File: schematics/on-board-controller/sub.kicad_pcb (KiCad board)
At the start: 2 copper layers, 90 x 60 mm, 40 parts, among them J1 5-1814832-1, J2 programmer, J3 xt60, M1 Motor_DC, M2 Motor_DC, M3 Stepper_Motor_bipolar, Q1 NMOS, Q2 NMOS, U1 L293D, U2 STM32L476RGTx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

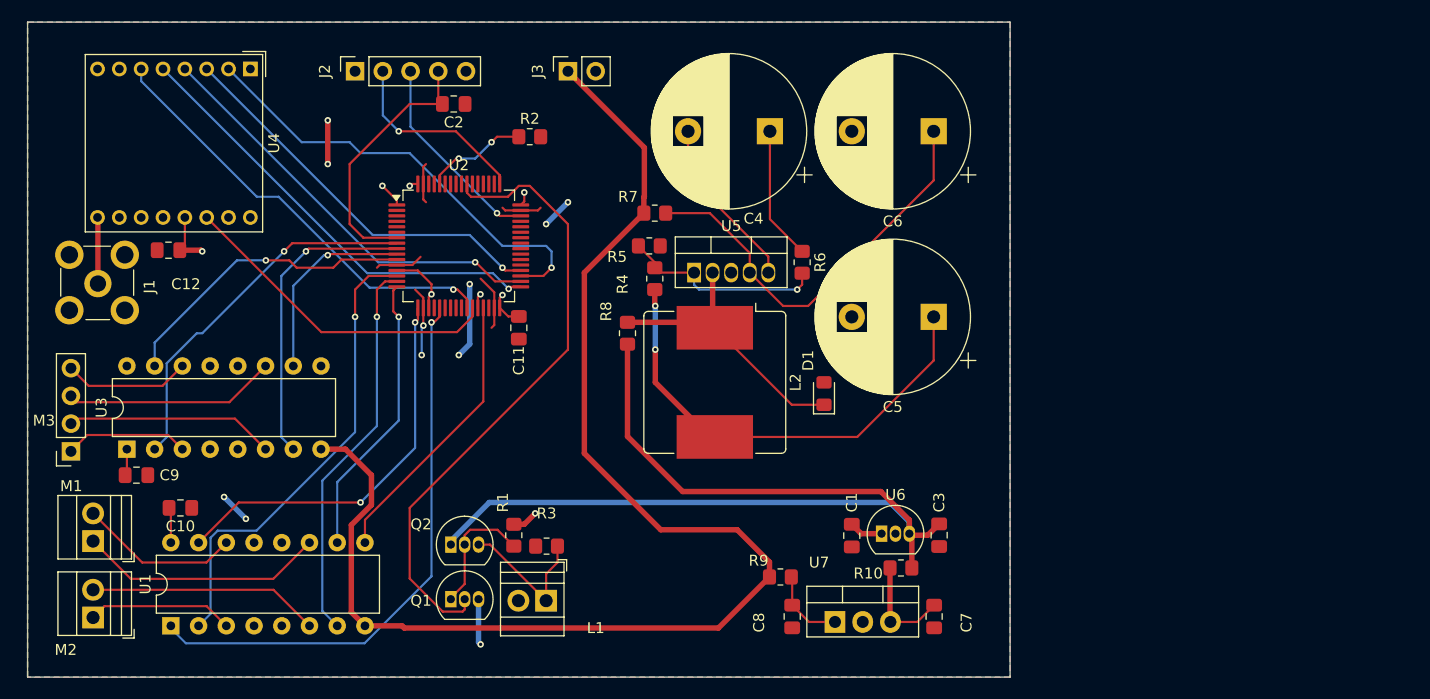
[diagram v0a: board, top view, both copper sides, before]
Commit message: new version, and ltspice for electromagnet
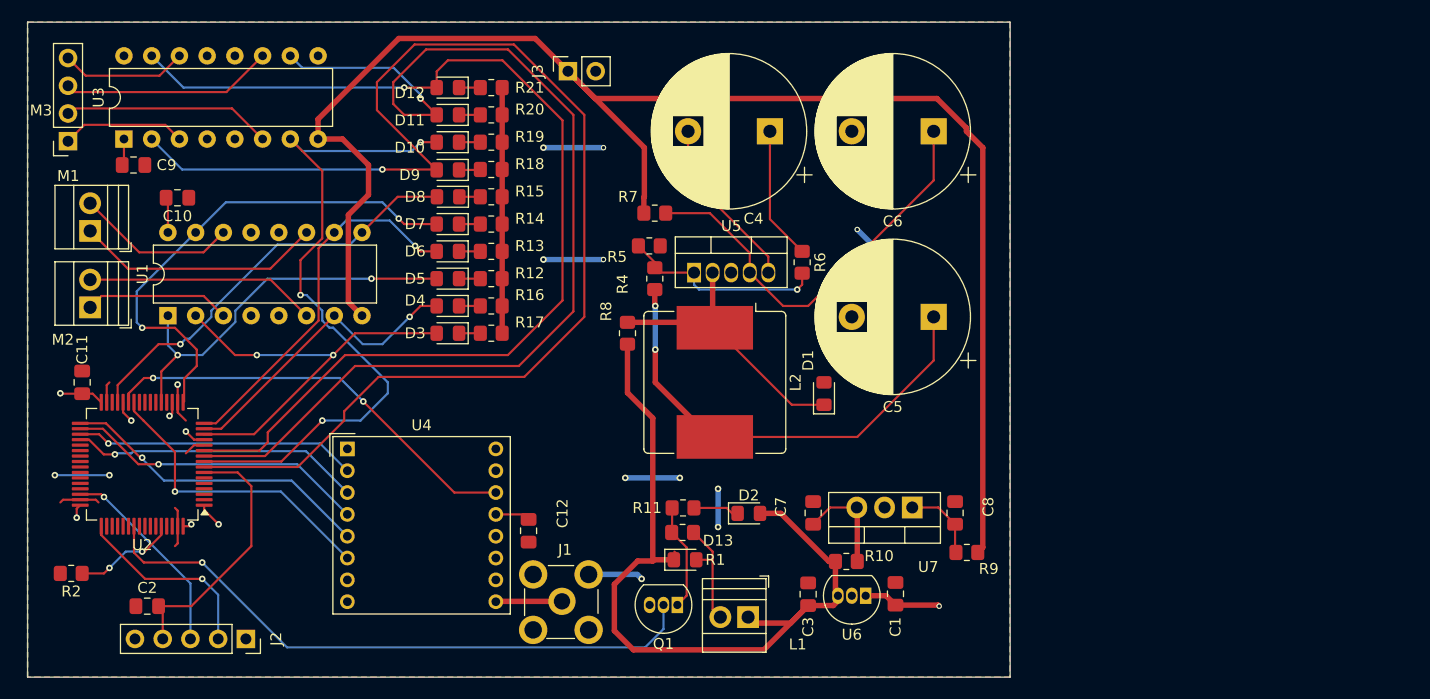
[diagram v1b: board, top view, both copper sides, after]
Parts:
- removed Q2: NMOS, Package_TO_SOT_THT:TO-92_Inline
- removed R3: 10k, Resistor_SMD:R_0805_2012Metric_Pad1.20x1.40mm_HandSolder
- added D10: LED, LED_SMD:LED_0805_2012Metric_Pad1.15x1.40mm_HandSolder, F.Cu at (101.5, 71.5)
- added D11: LED, LED_SMD:LED_0805_2012Metric_Pad1.15x1.40mm_HandSolder, F.Cu at (101.5, 69.0)
- added D12: LED, LED_SMD:LED_0805_2012Metric_Pad1.15x1.40mm_HandSolder, F.Cu at (101.5, 66.5)
- added D13: D, LED_SMD:LED_0805_2012Metric_Pad1.15x1.40mm_HandSolder, F.Cu at (123.2, 109.8)
- added D2: LED, LED_SMD:LED_0805_2012Metric_Pad1.15x1.40mm_HandSolder, F.Cu at (129.1, 105.5)
- added D3: LED, LED_SMD:LED_0805_2012Metric_Pad1.15x1.40mm_HandSolder, F.Cu at (101.5, 89.0)
- added D4: LED, LED_SMD:LED_0805_2012Metric_Pad1.15x1.40mm_HandSolder, F.Cu at (101.5, 86.5)
- added D5: LED, LED_SMD:LED_0805_2012Metric_Pad1.15x1.40mm_HandSolder, F.Cu at (101.5, 84.0)
- added D6: LED, LED_SMD:LED_0805_2012Metric_Pad1.15x1.40mm_HandSolder, F.Cu at (101.5, 81.5)
- added D7: LED, LED_SMD:LED_0805_2012Metric_Pad1.15x1.40mm_HandSolder, F.Cu at (101.5, 79.0)
- added D8: LED, LED_SMD:LED_0805_2012Metric_Pad1.15x1.40mm_HandSolder, F.Cu at (101.5, 76.5)
- added D9: LED, LED_SMD:LED_0805_2012Metric_Pad1.15x1.40mm_HandSolder, F.Cu at (101.5, 74.0)
- added R11: 330, Resistor_SMD:R_0805_2012Metric_Pad1.20x1.40mm_HandSolder, F.Cu at (123.0, 105.0)
- added R12: 330, Resistor_SMD:R_0805_2012Metric_Pad1.20x1.40mm_HandSolder, F.Cu at (105.5, 84.0)
- added R13: 330, Resistor_SMD:R_0805_2012Metric_Pad1.20x1.40mm_HandSolder, F.Cu at (105.5, 81.5)
- added R14: 330, Resistor_SMD:R_0805_2012Metric_Pad1.20x1.40mm_HandSolder, F.Cu at (105.5, 79.0)
- added R15: 330, Resistor_SMD:R_0805_2012Metric_Pad1.20x1.40mm_HandSolder, F.Cu at (105.5, 76.5)
- added R16: 330, Resistor_SMD:R_0805_2012Metric_Pad1.20x1.40mm_HandSolder, F.Cu at (105.5, 86.5)
- added R17: 330, Resistor_SMD:R_0805_2012Metric_Pad1.20x1.40mm_HandSolder, F.Cu at (105.5, 89.0)
- added R18: 330, Resistor_SMD:R_0805_2012Metric_Pad1.20x1.40mm_HandSolder, F.Cu at (105.5, 74.0)
- added R19: 330, Resistor_SMD:R_0805_2012Metric_Pad1.20x1.40mm_HandSolder, F.Cu at (105.5, 71.5)
- added R20: 330, Resistor_SMD:R_0805_2012Metric_Pad1.20x1.40mm_HandSolder, F.Cu at (105.5, 69.0)
- added R21: 330, Resistor_SMD:R_0805_2012Metric_Pad1.20x1.40mm_HandSolder, F.Cu at (105.5, 66.5)
- R1: value 10k -> 6
- moved R2 58.0 mm to (67.0, 111.0), turned to 180 degrees
- moved C2 53.9 mm to (74.0, 114.0), turned to 0 degrees
- moved J2 53.0 mm to (83.0, 117.0), turned to -90 degrees
- moved J1 51.6 mm to (111.9, 113.6), turned to 0 degrees
- moved C12 41.8 mm to (108.9, 107.1), turned to 90 degrees
- moved C11 40.3 mm to (68.0, 93.5), turned to -90 degrees
- moved U4 35.9 mm to (92.3, 99.6), turned to 0 degrees
- moved U2 35.2 mm to (73.5, 101.0), turned to 180 degrees
- moved M1 28.4 mm to (68.7, 79.6)
- moved M2 28.4 mm to (68.7, 86.6)
- moved U3 28.4 mm to (71.8, 71.2)
- moved C10 28.4 mm to (76.7, 76.6)
- moved C9 28.4 mm to (72.7, 73.6)
- moved M3 28.4 mm to (66.7, 71.4)
- moved U1 28.4 mm to (75.9, 87.4)
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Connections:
- L1 pad 1: Net-(L1--) -> +6V
- L1 pad 2: GND -> Net-(D13-A)
- R1 pad 1: +3V3 -> Net-(D13-A)
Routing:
- net STEPPER1: track 34.0 -> 120.2 mm
- net STEPPER3: track 18.0 -> 99.8 mm
- net STEPPER4: track 28.0 -> 98.6 mm
- net STEPPER2: track 27.9 -> 62.8 mm, vias 1 -> 3
- net GND: track 40.1 -> 70.7 mm, vias 9 -> 14
- net +BATT: track 122.5 -> 144.1 mm
- net +6V: track 90.8 -> 72.6 mm
- net DC_MOTOR_EN1_2: track 52.2 -> 36.4 mm, vias 1 -> 2
- net MISO: track 41.1 -> 25.9 mm
- net Net-(L1--): track 13.7 -> 0.00 mm
- net NSS: track 41.2 -> 28.8 mm
- net DC_MOTOR_EN3_4: track 26.0 -> 38.3 mm, vias 0 -> 1
- net RESET_RADIO: track 40.0 -> 28.0 mm
- net SCK: track 38.8 -> 27.7 mm
- net Net-(D13-A): track 0.00 -> 10.3 mm
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
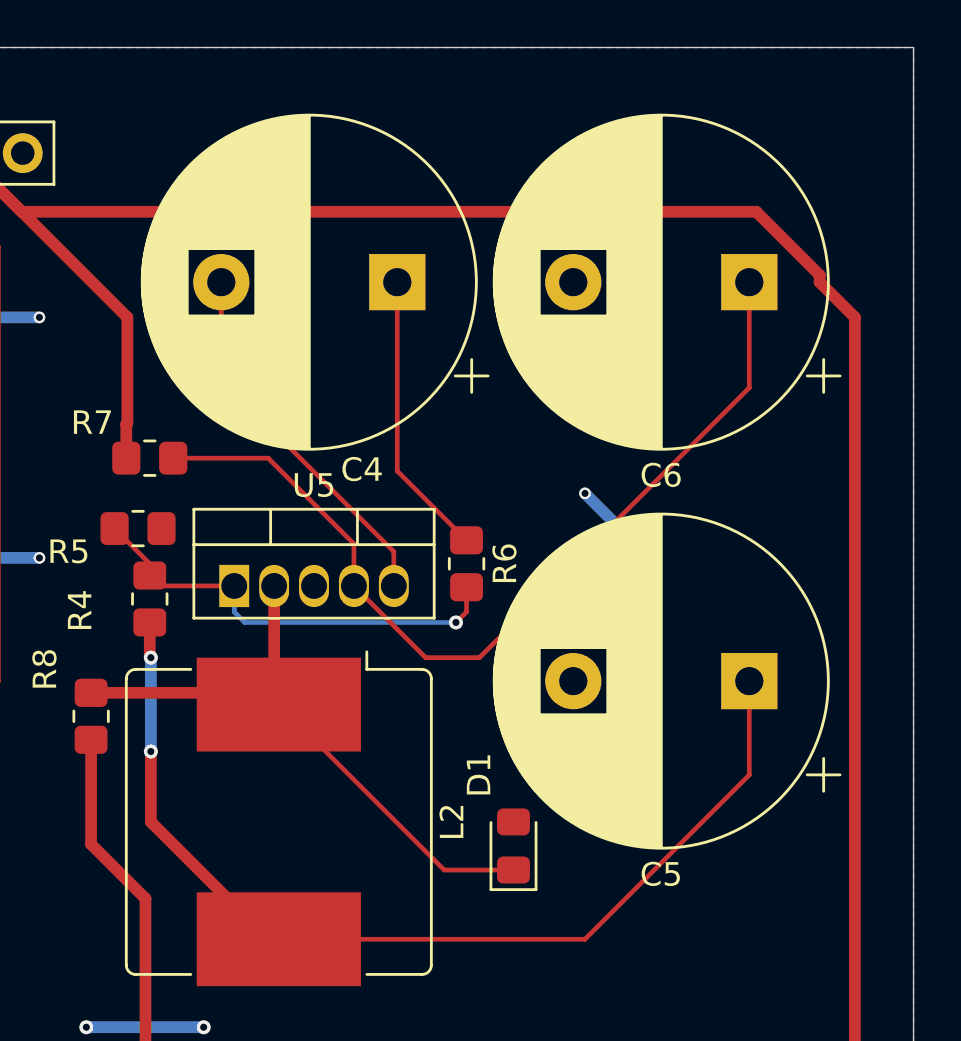
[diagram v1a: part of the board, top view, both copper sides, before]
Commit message: changed size of electrolytic capacitors
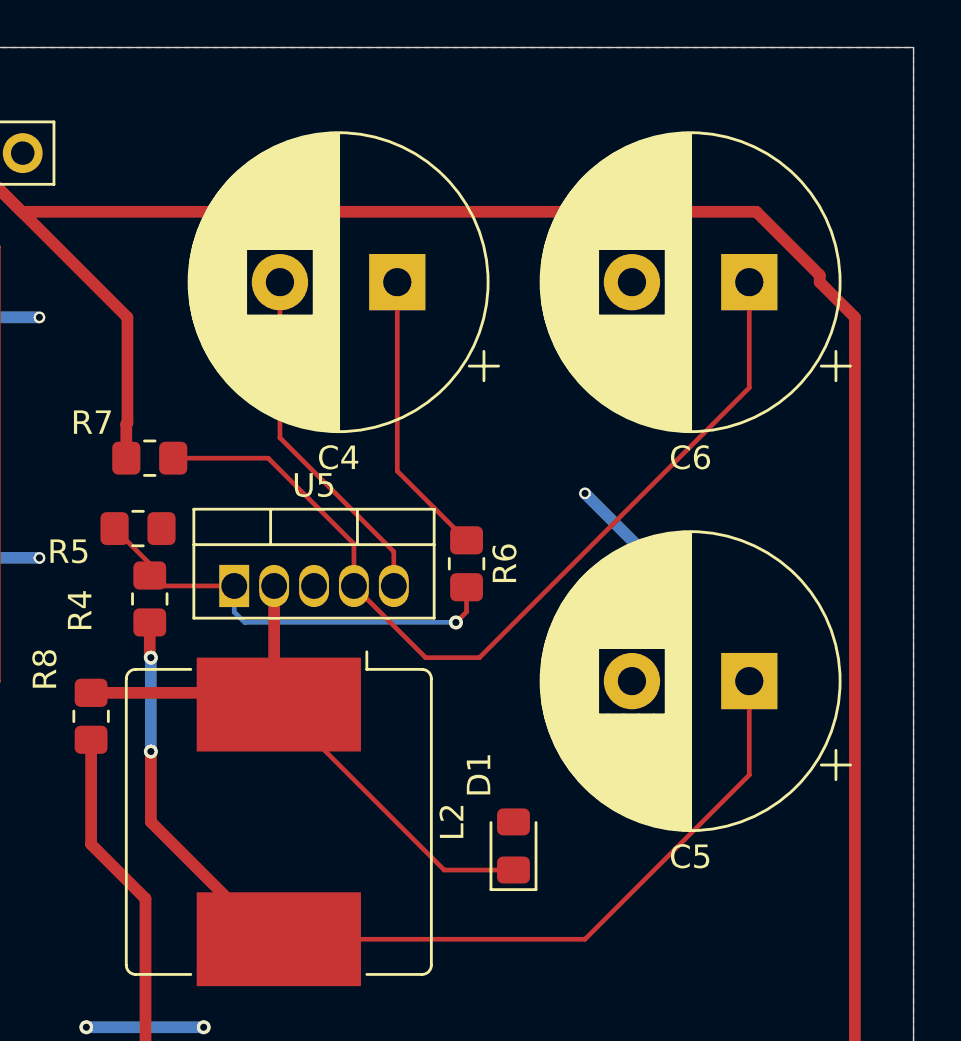
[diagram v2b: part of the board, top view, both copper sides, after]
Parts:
- C4, C5, C6: footprint Capacitor_THT:CP_Radial_D14.0mm_P7.50mm -> Capacitor_THT:CP_Radial_D12.5mm_P5.00mm
- R1: value 6 -> 10
- R11: value 330 -> 1k
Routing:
- net Net-(U5-COMPENSATION): track 16.0 -> 15.0 mm

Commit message: updated names of components on schematic
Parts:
- U5: value ~ -> MC34166TG
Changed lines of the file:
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@@
 			(outputformat 1)
 			(mirror no)
-			(drillshape 1)
+			(drillshape 0)
 			(scaleselection 1)
 			(outputdirectory "")
@@
 			)
 		)
-		(property "Value" "~"
+		(property "Value" "MC34166TG"
 			(at 0 0 0)
 			(layer "F.Fab")

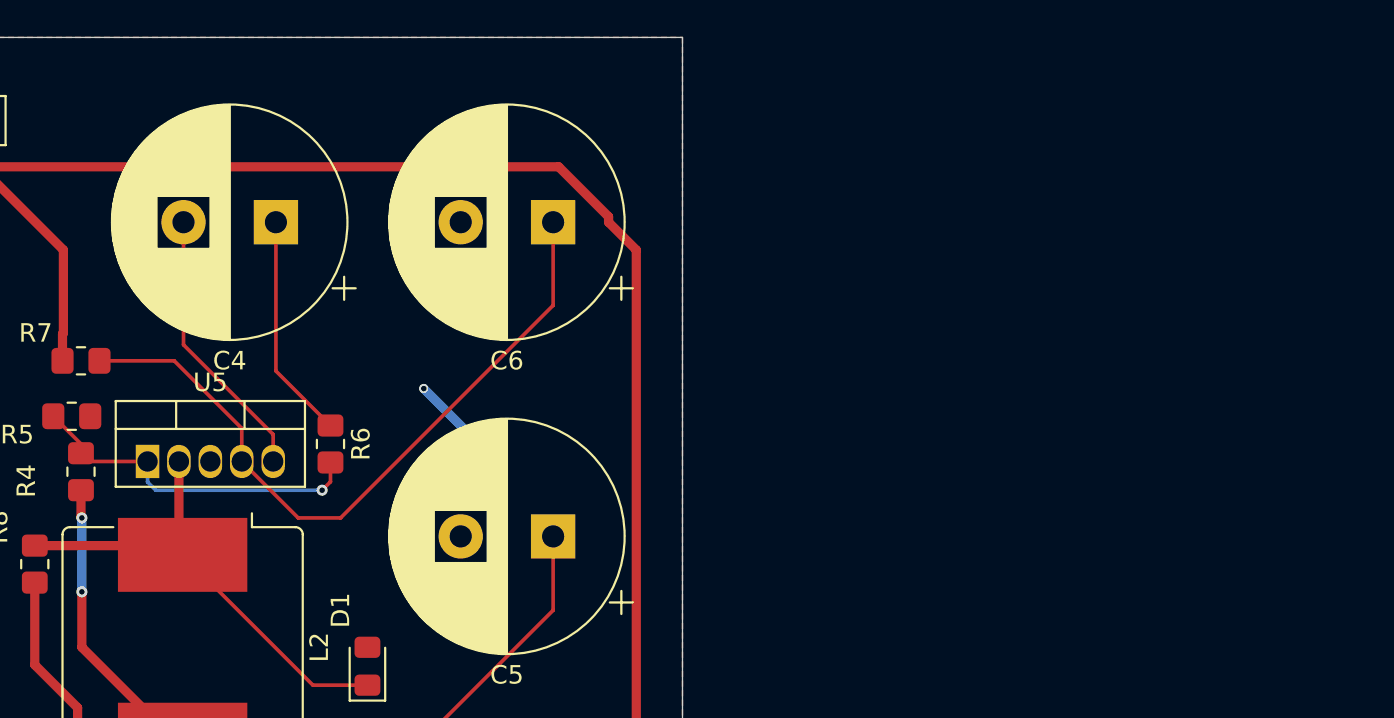
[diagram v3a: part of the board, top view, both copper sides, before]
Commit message: updated on-board schematic with changes
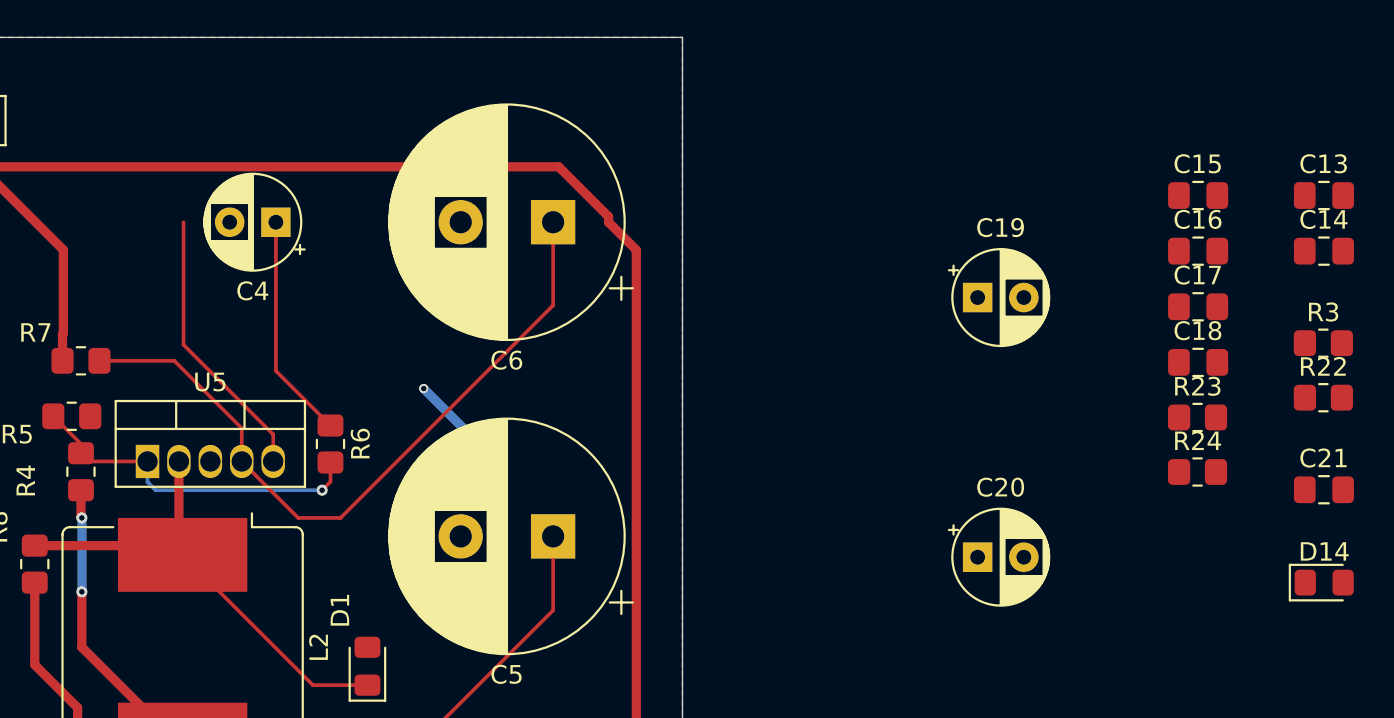
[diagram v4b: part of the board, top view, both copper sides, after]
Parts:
- added C13: 100n, Capacitor_SMD:C_0805_2012Metric_Pad1.18x1.45mm_HandSolder, F.Cu at (187.7, 69.1)
- added C14: 100n, Capacitor_SMD:C_0805_2012Metric_Pad1.18x1.45mm_HandSolder, F.Cu at (187.7, 72.1)
- added C15: 100n, Capacitor_SMD:C_0805_2012Metric_Pad1.18x1.45mm_HandSolder, F.Cu at (180.9, 69.1)
- added C16: 100n, Capacitor_SMD:C_0805_2012Metric_Pad1.18x1.45mm_HandSolder, F.Cu at (180.9, 72.1)
- added C17: 100n, Capacitor_SMD:C_0805_2012Metric_Pad1.18x1.45mm_HandSolder, F.Cu at (180.9, 75.1)
- added C18: 100n, Capacitor_SMD:C_0805_2012Metric_Pad1.18x1.45mm_HandSolder, F.Cu at (180.9, 78.1)
- added C19: 10u, Capacitor_THT:CP_Radial_D5.0mm_P2.50mm, F.Cu at (169.0, 74.6)
- added C20: 10u, Capacitor_THT:CP_Radial_D5.0mm_P2.50mm, F.Cu at (169.0, 88.6)
- added C21: 100n, Capacitor_SMD:C_0805_2012Metric_Pad1.18x1.45mm_HandSolder, F.Cu at (187.7, 85.0)
- added D14: D, LED_SMD:LED_0805_2012Metric_Pad1.15x1.40mm_HandSolder, F.Cu at (187.7, 90.0)
- added R22: 1k, Resistor_SMD:R_0805_2012Metric_Pad1.20x1.40mm_HandSolder, F.Cu at (187.7, 80.0)
- added R23: 4k7, Resistor_SMD:R_0805_2012Metric_Pad1.20x1.40mm_HandSolder, F.Cu at (180.9, 81.1)
- added R24: 4k7, Resistor_SMD:R_0805_2012Metric_Pad1.20x1.40mm_HandSolder, F.Cu at (180.9, 84.0)
- added R3: 4k7, Resistor_SMD:R_0805_2012Metric_Pad1.20x1.40mm_HandSolder, F.Cu at (187.7, 77.0)
- C4: footprint Capacitor_THT:CP_Radial_D12.5mm_P5.00mm -> Capacitor_THT:CP_Radial_D5.0mm_P2.50mm
- R2: value 100k -> 10k
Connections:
- J3 pad 1: +BATT -> Net-(D14-A)
- Q1 pad 2: ELECTROMAGNET -> Net-(Q1-G)
- R8 pad 1: Net-(D1-K) -> Net-(C5-Pad1)
- U1 pad 16: +3V3 -> +6V
- U3 pad 1: +3V3 -> +6V
- U3 pad 16: +3V3 -> +6V
- U3 pad 9: +3V3 -> +6V

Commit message: some layout updates
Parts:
- moved D14 78.1 mm to (113.8, 65.0)
- moved C21 26.8 mm to (164.5, 98.2)
- moved J3 6.01 mm to (118.5, 64.7)
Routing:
- net Net-(D14-A): track 0.00 -> 3.84 mm
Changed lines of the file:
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@@
 	(footprint "Connector_PinSocket_2.54mm:PinSocket_1x02_P2.54mm_Vertical"
 		(layer "F.Cu")
-		(at 112.5 65 90)
+		(at 118.5 64.725 90)
 		(descr "Through hole straight socket strip, 1x02, 2.54mm pitch, single row (from Kicad 4.0.7), script generated")
 		(tags "Through hole socket strip THT 1x02 2.54mm single row")
 		(property "Reference" "J3"
-			(at 0 -2.77 90)
+			(at 1.475 -2.5 90)
 			(layer "F.SilkS")
 			(effects
@@
 	(footprint "Capacitor_SMD:C_0805_2012Metric_Pad1.18x1.45mm_HandSolder"
 		(layer "F.Cu")
-		(at 187.71 84.975)
+		(at 164.4625 98.25)
 		(descr "Capacitor SMD 0805 (2012 Metric), square (rectangular) end terminal, IPC_7351 nominal with elongated pad for handsoldering. (Body size source: IPC-SM-782 page 76, https://www.pcb-3d.com/wordpress/wp-content/uploads/ipc-sm-782a_amendment_1_and_2.pdf, https://docs.google.com/spreadsheets/d/1BsfQQcO9C6DZCsRaXUlFlo91Tg2WpOkGARC1WS5S8t0/edit?usp=sharing), generated with kicad-footprint-generator")
 		(tags "capacitor handsolder")
@@
 	(footprint "LED_SMD:LED_0805_2012Metric_Pad1.15x1.40mm_HandSolder"
 		(layer "F.Cu")
-		(at 187.725 90)
+		(at 113.75 65)
 		(descr "LED SMD 0805 (2012 Metric), square (rectangular) end terminal, IPC_7351 nominal, (Body size source: https://docs.google.com/spreadsheets/d/1BsfQQcO9C6DZCsRaXUlFlo91Tg2WpOkGARC1WS5S8t0/edit?usp=sharing), generated with kicad-footprint-generator")
 		(tags "LED handsolder")
 		(property "Reference" "D14"
-			(at 0 -1.65 0)
+			(at 0 -1.65 360)
 			(layer "F.SilkS")
 			(effects
@@
 		)
 		(property "Value" "D"
-			(at 0 1.65 0)
+			(at 0 1.65 360)
 			(layer "F.Fab")
 			(effects
@@
 		)
 		(fp_text user "${REFERENCE}"
-			(at 0 0 0)
+			(at 0 0 360)
 			(layer "F.Fab")
 			(effects
@@
 		(net 91)
 	)
+	(segment
+		(start 118.225 65)
+		(end 118.5 64.725)
+		(width 0.5)
+		(layer "F.Cu")
+		(net 92)
+	)
+	(segment
+		(start 114.775 65)
+		(end 118.225 65)
+		(width 0.5)
+		(layer "F.Cu")
+		(net 92)
+	)
 	(zone

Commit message: created new version of layout
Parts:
- moved R3 121.8 mm to (68.0, 99.8), turned to 180 degrees
- moved R22 117.1 mm to (72.5, 101.3), turned to 180 degrees
- moved C15 112.9 mm to (68.4, 78.2)
- moved C16 107.0 mm to (74.1, 65.3), turned to -90 degrees
- moved C18 91.0 mm to (90.4, 87.7), turned to -90 degrees
- moved C13 86.6 mm to (107.3, 101.5), turned to -90 degrees
- moved C17 85.3 mm to (95.6, 74.8), turned to -90 degrees
- moved R24 80.6 mm to (101.0, 73.0), turned to 180 degrees
- moved C19 75.8 mm to (94.4, 88.2), turned to 90 degrees
- moved C14 74.8 mm to (119.9, 103.5), turned to 180 degrees
- moved C20 74.0 mm to (97.1, 71.0), turned to 90 degrees
- moved R23 66.2 mm to (115.0, 74.5), turned to -90 degrees
- moved L1 59.8 mm to (69.3, 111.5), turned to 90 degrees
- moved U4 58.1 mm to (150.4, 101.3), turned to -90 degrees
- moved C9 57.6 mm to (109.3, 118.0), turned to 90 degrees
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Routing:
- net +6V: track 72.9 -> 188.7 mm
- net +BATT: track 144.1 -> 65.3 mm, vias 0 -> 1
- net GND: track 70.7 -> 139.8 mm, vias 14 -> 18
- net DC_MOTOR1: track 39.2 -> 107.7 mm, vias 2 -> 1
- net DC_MOTOR3: track 34.1 -> 94.8 mm
- net DC_MOTOR4: track 46.4 -> 105.8 mm, vias 2 -> 1
- net DC_MOTOR_EN1_2: track 36.4 -> 87.0 mm
- net DC_MOTOR2: track 28.1 -> 77.2 mm
- net STEPPER1: track 120.2 -> 72.5 mm
- net STEPPER3: track 99.8 -> 61.7 mm
- net DC_MOTOR_EN3_4: track 38.3 -> 69.0 mm, vias 1 -> 2
- net Net-(U5-INPUT): track 38.4 -> 21.8 mm
- net Net-(D1-K): track 26.3 -> 13.6 mm
- net STEPPER4: track 98.6 -> 86.3 mm
- net Net-(C5-Pad1): track 43.0 -> 31.1 mm, vias 2 -> 0
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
